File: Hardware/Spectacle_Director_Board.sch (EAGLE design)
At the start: 66 parts, among them J2 I2C-TRRS, J3 Serial-TRRS, Q1 310mA/60V/1.6Ω, Q2 310mA/60V/1.6Ω, U1 AP2151, U2 ATSAMD21G-A, U3 3.3V, U4 W25Q32FV

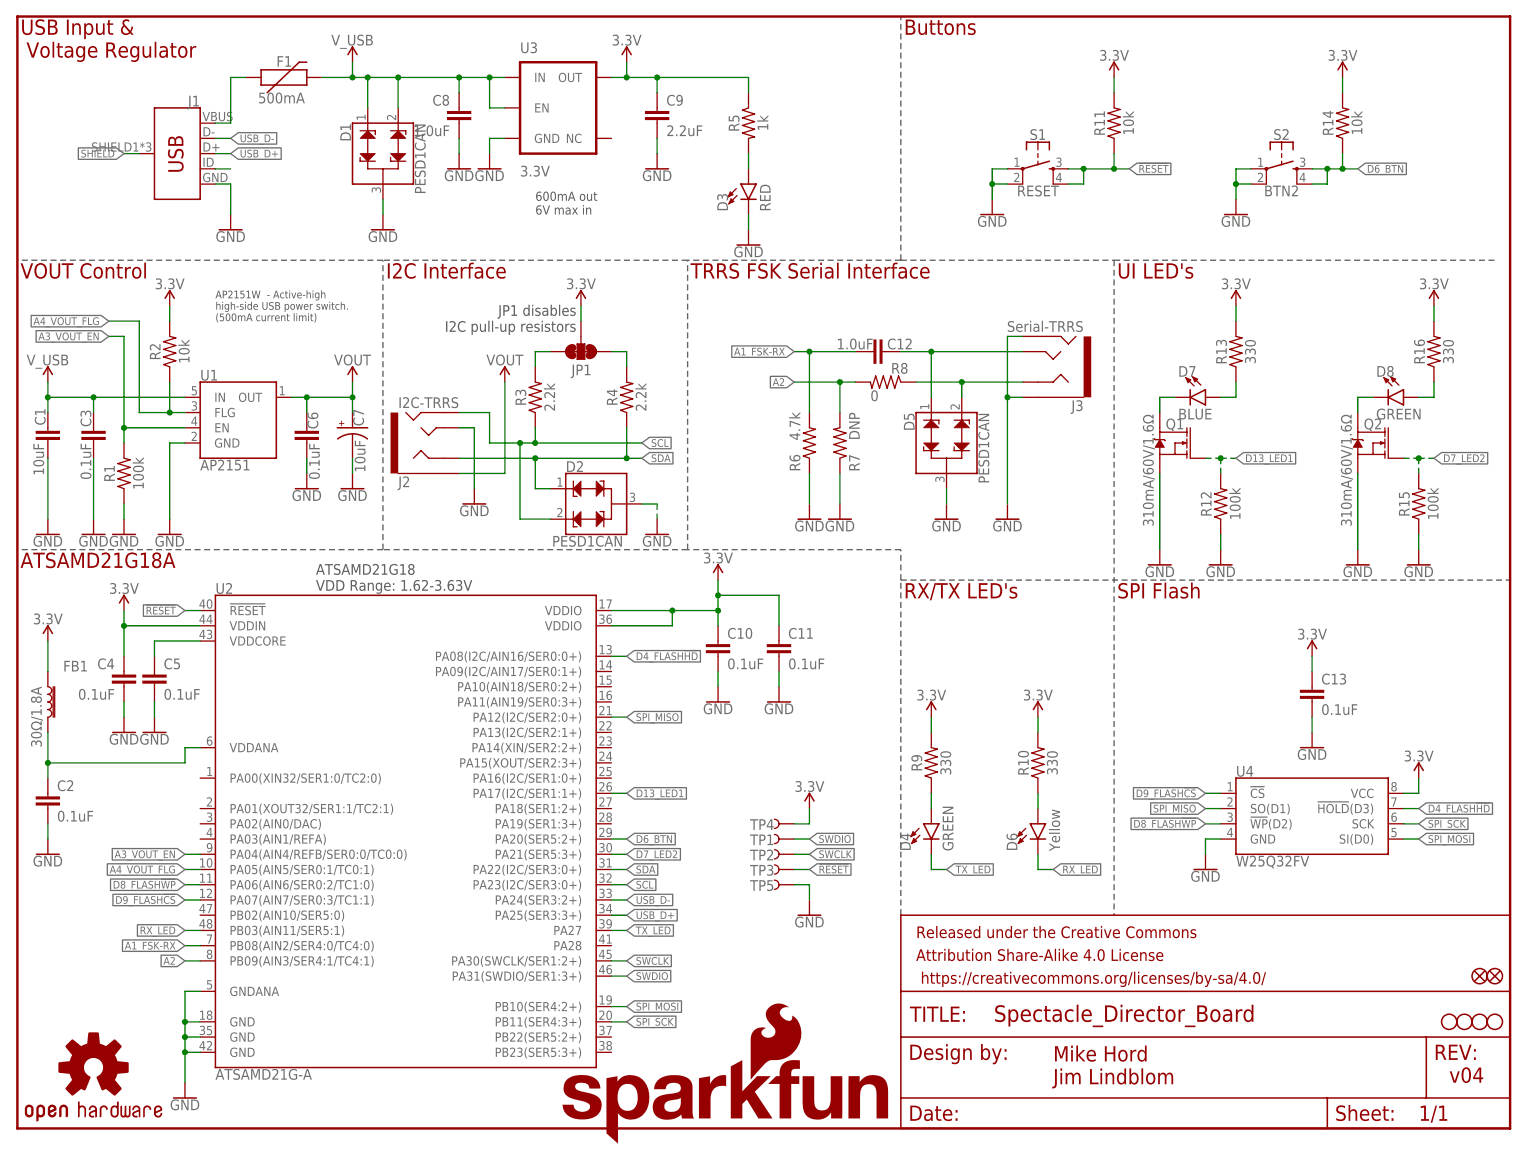
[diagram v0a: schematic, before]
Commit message: Added FSK demodulation hardware Changed pin assignment of FSK channel to channel with comparator Moved power switch FAULT line to a different pin
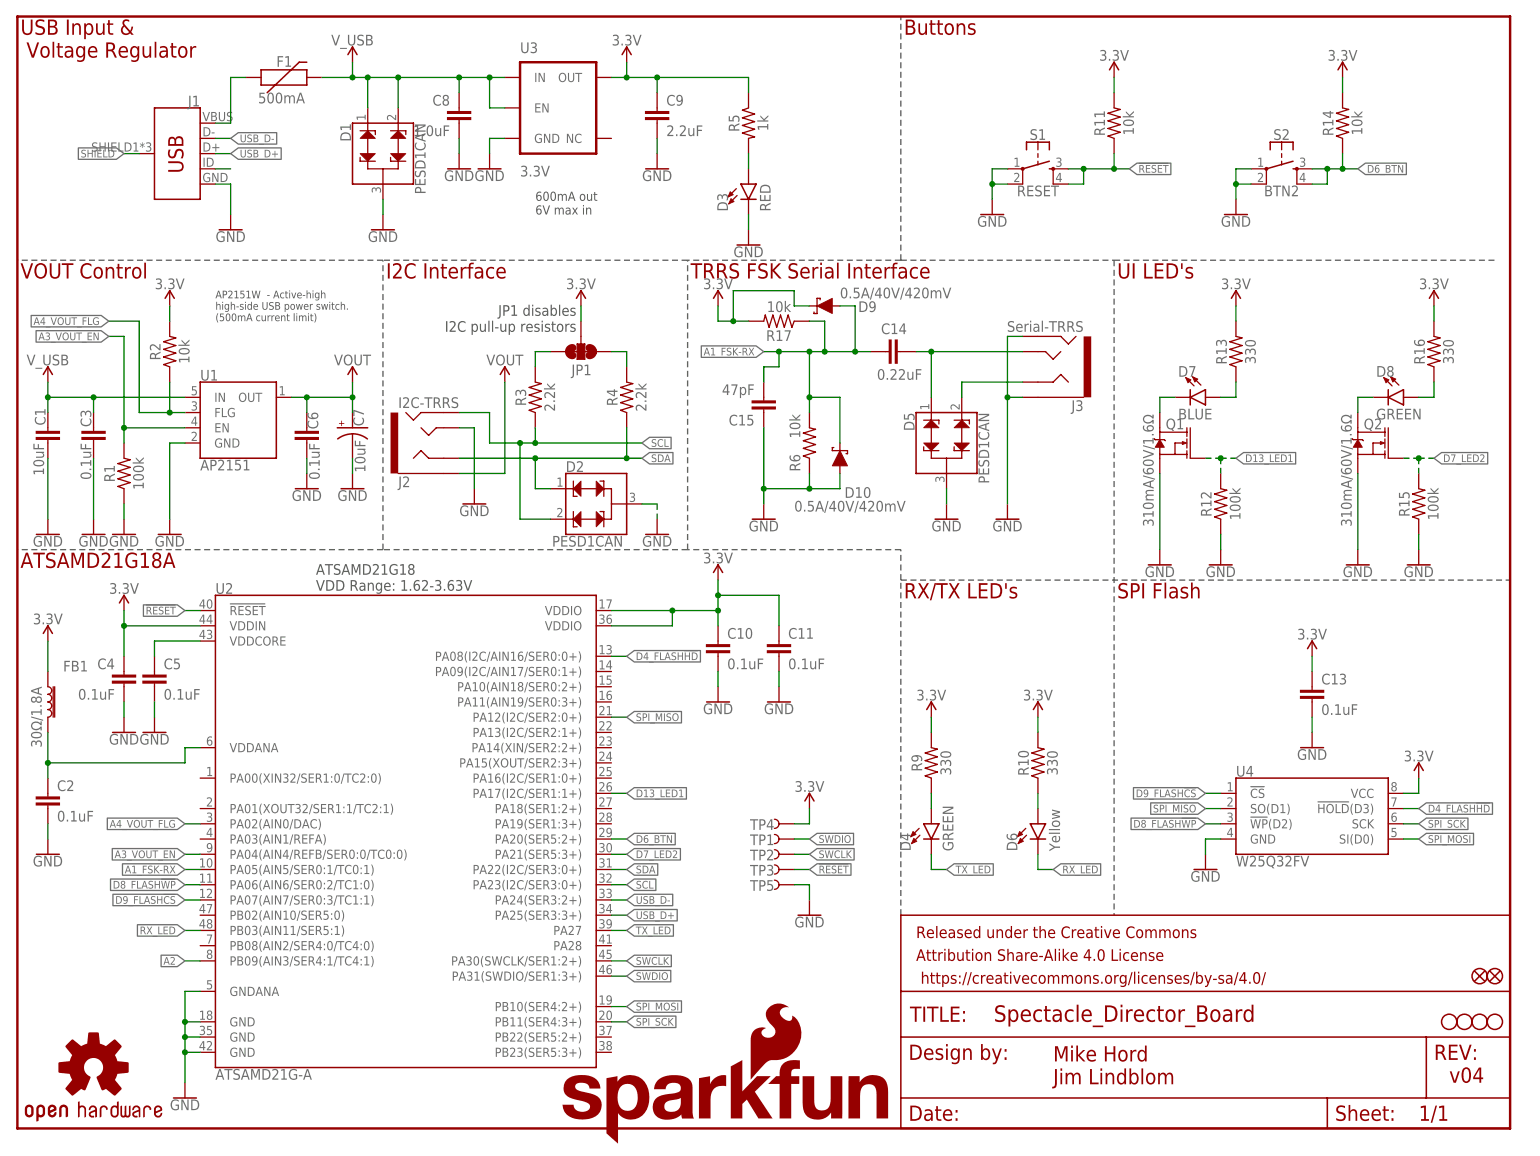
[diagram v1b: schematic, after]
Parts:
- removed C12: 1.0uF, SparkFun-Capacitors:1.0UF-0603-16V-10%
- removed R7: DNP, SparkFun-Resistors:4.7KOHM-0603-1/10W-1%
- removed R8: 0, SparkFun-Resistors:0OHM-0603-1/10W-5%
- added C14: 0.22uF, SparkFun-Capacitors:0.22UF-0603-25V-10%
- added C15: 47pF, SparkFun-Capacitors:47PF-0603-50V-5%
- added D10, D9: 0.5A/40V/420mV, SparkFun-DiscreteSemi:DIODE-SCHOTTKY-PMEG4005EJ
- added R17: 10k, SparkFun-Resistors:10KOHM-0603-1/10W-1%
- R6: value 4.7k -> 10k; device SparkFun-Resistors:4.7KOHM-0603-1/10W-1% -> SparkFun-Resistors:10KOHM-0603-1/10W-1%
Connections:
- net 3.3V: now also D9.C, R17.2
- net A1_FSK-RX: now also C14.1, C15.2, D10.C, D9.A, R17.1, U2.PA05(AIN5/SER0:1/TC0:1); no longer C12.2, U2.PB08(AIN2/SER4:0/TC4:0)
- net A2: no longer R7.2, R8.2
- net A4_VOUT_FLG: now also U2.PA02(AIN0/DAC); no longer U2.PA05(AIN5/SER0:1/TC0:1)
- net GND: now also C15.1, D10.A; no longer R7.1
- net RING1-RIGHT: no longer R8.1
- net TIP-LEFT: now also C14.2; no longer C12.1

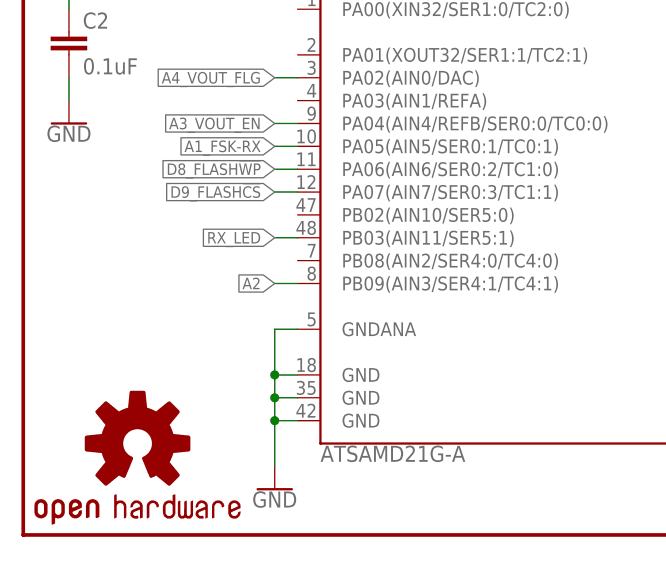
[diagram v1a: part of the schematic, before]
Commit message: FSK demodulation harware layout
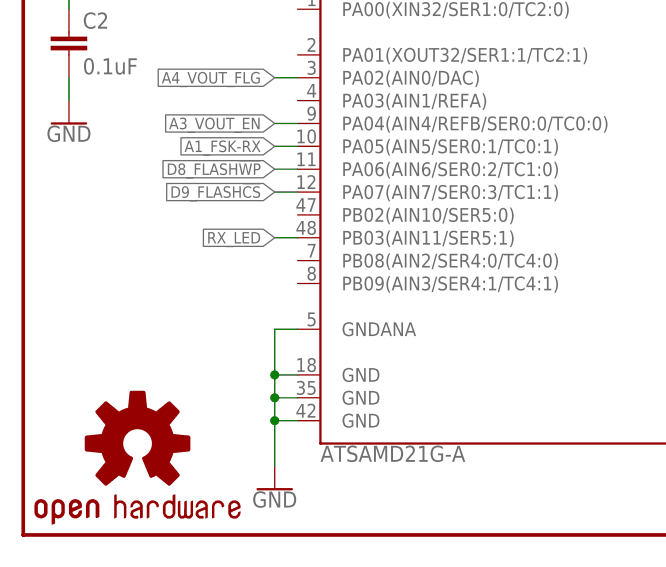
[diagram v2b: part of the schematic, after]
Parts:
- JP1: value JUMPER-SMT_3_2-NC_TRACE_SILK -> JUMPER-SMT_3_2-NC_TRACE_NO-SILK; device SparkFun-Jumpers:JUMPER-SMT_3_2-NC_TRACE_SILK -> SparkFun-Jumpers:JUMPER-SMT_3_2-NC_TRACE_NO-SILK
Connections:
- removed net A2: U2.PB09(AIN3/SER4:1/TC4:1)
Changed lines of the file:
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@@
 <grid distance="0.1" unitdist="inch" unit="inch" style="lines" multiple="1" display="no" altdistance="0.01" altunitdist="inch" altunit="inch"/>
 <layers>
-<layer number="1" name="Top" color="4" fill="1" visible="no" active="no"/>
-<layer number="2" name="Route2" color="1" fill="3" visible="no" active="no"/>
-<layer number="3" name="Route3" color="4" fill="3" visible="no" active="no"/>
-<layer number="4" name="Route4" color="1" fill="4" visible="no" active="no"/>
-<layer number="5" name="Route5" color="4" fill="4" visible="no" active="no"/>
-<layer number="6" name="Route6" color="1" fill="8" visible="no" active="no"/>
-<layer number="7" name="Route7" color="4" fill="8" visible="no" active="no"/>
-<layer number="8" name="Route8" color="1" fill="2" visible="no" active="no"/>
-<layer number="9" name="Route9" color="4" fill="2" visible="no" active="no"/>
-<layer number="10" name="Route10" color="1" fill="7" visible="no" active="no"/>
-<layer number="11" name="Route11" color="4" fill="7" visible="no" active="no"/>
-<layer number="12" name="Route12" color="1" fill="5" visible="no" active="no"/>
-<layer number="13" name="Route13" color="4" fill="5" visible="no" active="no"/>
-<layer number="14" name="Route14" color="1" fill="6" visible="no" active="no"/>
-<layer number="15" name="Route15" color="4" fill="6" visible="no" active="no"/>
-<layer number="16" name="Bottom" color="1" fill="1" visible="no" active="no"/>
-<layer number="17" name="Pads" color="2" fill="1" visible="no" active="no"/>
-<layer number="18" name="Vias" color="2" fill="1" visible="no" active="no"/>
-<layer number="19" name="Unrouted" color="6" fill="1" visible="no" active="no"/>
-<layer number="20" name="Dimension" color="15" fill="1" visible="no" active="no"/>
-<layer number="21" name="tPlace" color="16" fill="1" visible="no" active="no"/>
-<layer number="22" name="bPlace" color="14" fill="1" visible="no" active="no"/>
-<layer number="23" name="tOrigins" color="15" fill="1" visible="no" active="no"/>
-<layer number="24" name="bOrigins" color="15" fill="1" visible="no" active="no"/>
-<layer number="25" name="tNames" color="7" fill="1" visible="no" active="no"/>
-<layer number="26" name="bNames" color="7" fill="1" visible="no" active="no"/>
-<layer number="27" name="tValues" color="7" fill="1" visible="no" active="no"/>
-<layer number="28" name="bValues" color="7" fill="1" visible="no" active="no"/>
+<layer number="1" name="Top" color="4" fill="1" visible="yes" active="no"/>
+<layer number="2" name="Route2" color="1" fill="3" visible="yes" active="no"/>
+<layer number="3" name="Route3" color="4" fill="3" visible="yes" active="no"/>
+<layer number="4" name="Route4" color="1" fill="4" visible="yes" active="no"/>
+<layer number="5" name="Route5" color="4" fill="4" visible="yes" active="no"/>
+<layer number="6" name="Route6" color="1" fill="8" visible="yes" active="no"/>
+<layer number="7" name="Route7" color="4" fill="8" visible="yes" active="no"/>
+<layer number="8" name="Route8" color="1" fill="2" visible="yes" active="no"/>
+<layer number="9" name="Route9" color="4" fill="2" visible="yes" active="no"/>
+<layer number="10" name="Route10" color="1" fill="7" visible="yes" active="no"/>
+<layer number="11" name="Route11" color="4" fill="7" visible="yes" active="no"/>
+<layer number="12" name="Route12" color="1" fill="5" visible="yes" active="no"/>
+<layer number="13" name="Route13" color="4" fill="5" visible="yes" active="no"/>
+<layer number="14" name="Route14" color="1" fill="6" visible="yes" active="no"/>
+<layer number="15" name="Route15" color="4" fill="6" visible="yes" active="no"/>
+<layer number="16" name="Bottom" color="1" fill="1" visible="yes" active="no"/>
+<layer number="17" name="Pads" color="2" fill="1" visible="yes" active="no"/>
+<layer number="18" name="Vias" color="2" fill="1" visible="yes" active="no"/>
+<layer number="19" name="Unrouted" color="6" fill="1" visible="yes" active="no"/>
+<layer number="20" name="Dimension" color="15" fill="1" visible="yes" active="no"/>
+<layer number="21" name="tPlace" color="16" fill="1" visible="yes" active="no"/>
+<layer number="22" name="bPlace" color="14" fill="1" visible="yes" active="no"/>
+<layer number="23" name="tOrigins" color="15" fill="1" visible="yes" active="no"/>
+<layer number="24" name="bOrigins" color="15" fill="1" visible="yes" active="no"/>
+<layer number="25" name="tNames" color="7" fill="1" visible="yes" active="no"/>
+<layer number="26" name="bNames" color="7" fill="1" visible="yes" active="no"/>
+<layer number="27" name="tValues" color="7" fill="1" visible="yes" active="no"/>
+<layer number="28" name="bValues" color="7" fill="1" visible="yes" active="no"/>
 <layer number="29" name="tStop" color="7" fill="3" visible="no" active="no"/>
 <layer number="30" name="bStop" color="7" fill="6" visible="no" active="no"/>
@@
 <layer number="35" name="tGlue" color="7" fill="4" visible="no" active="no"/>
 <layer number="36" name="bGlue" color="7" fill="5" visible="no" active="no"/>
-<layer number="37" name="tTest" color="7" fill="1" visible="no" active="no"/>
-<layer number="38" name="bTest" color="7" fill="1" visible="no" active="no"/>
+<layer number="37" name="tTest" color="7" fill="1" visible="yes" active="no"/>
+<layer number="38" name="bTest" color="7" fill="1" visible="yes" active="no"/>
 <layer number="39" name="tKeepout" color="16" fill="11" visible="no" active="no"/>
 <layer number="40" name="bKeepout" color="1" fill="11" visible="no" active="no"/>
@@
 <layer number="44" name="Drills" color="7" fill="1" visible="no" active="no"/>
 <layer number="45" name="Holes" color="7" fill="1" visible="no" active="no"/>
-<layer number="46" name="Milling" color="3" fill="1" visible="no" active="no"/>
-<layer number="47" name="Measures" color="7" fill="1" visible="no" active="no"/>
-<layer number="48" name="Document" color="7" fill="1" visible="no" active="no"/>
-<layer number="49" name="Reference" color="7" fill="1" visible="no" active="no"/>
-<layer number="50" name="dxf" color="7" fill="1" visible="no" active="no"/>
-<layer number="51" name="tDocu" color="6" fill="1" visible="no" active="no"/>
-<layer number="52" name="bDocu" color="7" fill="1" visible="no" active="no"/>
-<layer number="53" name="tGND_GNDA" color="7" fill="9" visible="no" active="no"/>
-<layer number="54" name="bGND_GNDA" color="1" fill="9" visible="no" active="no"/>
-<layer number="56" name="wert" color="7" fill="1" visible="no" active="no"/>
-<layer number="57" name="tCAD" color="7" fill="1" visible="no" active="no"/>
-<layer number="59" name="tCarbon" color="7" fill="1" visible="no" active="no"/>
-<layer number="60" name="bCarbon" color="7" fill="1" visible="no" active="no"/>
+<layer number="46" name="Milling" color="3" fill="1" visible="yes" active="no"/>
+<layer number="47" name="Measures" color="7" fill="1" visible="yes" active="no"/>
+<layer number="48" name="Document" color="7" fill="1" visible="yes" active="no"/>
+<layer number="49" name="Reference" color="7" fill="1" visible="yes" active="no"/>
+<layer number="50" name="dxf" color="7" fill="1" visible="yes" active="no"/>
+<layer number="51" name="tDocu" color="6" fill="1" visible="yes" active="no"/>
+<layer number="52" name="bDocu" color="7" fill="1" visible="yes" active="no"/>
+<layer number="53" name="tGND_GNDA" color="7" fill="9" visible="yes" active="no"/>
+<layer number="54" name="bGND_GNDA" color="1" fill="9" visible="yes" active="no"/>
+<layer number="56" name="wert" color="7" fill="1" visible="yes" active="no"/>
+<layer number="57" name="tCAD" color="7" fill="1" visible="yes" active="no"/>
+<layer number="59" name="tCarbon" color="7" fill="1" visible="yes" active="no"/>
+<layer number="60" name="bCarbon" color="7" fill="1" visible="yes" active="no"/>
 <layer number="90" name="Modules" color="5" fill="1" visible="yes" active="yes"/>
 <layer number="91" name="Nets" color="2" fill="1" visible="yes" active="yes"/>
@@
 <part name="R3" library="SparkFun-Resistors" deviceset="2.2KOHM" device="-0603-1/10W-1%" value="2.2k"/>
 <part name="R4" library="SparkFun-Resistors" deviceset="2.2KOHM" device="-0603-1/10W-1%" value="2.2k"/>
-<part name="JP1" library="SparkFun-Jumpers" deviceset="JUMPER-SMT_3_2-NC_TRACE" device="_SILK"/>
+<part name="JP1" library="SparkFun-Jumpers" deviceset="JUMPER-SMT_3_2-NC_TRACE" device="_NO-SILK" value="JUMPER-SMT_3_2-NC_TRACE_NO-SILK"/>
 <part name="SUPPLY8" library="SparkFun-PowerSymbols" deviceset="3.3V" device=""/>
 <part name="D2" library="SparkFun-DiscreteSemi" deviceset="PESD1CAN" device=""/>
@@
 </segment>
 </net>
-<net name="A2" class="0">
-<segment>
-<pinref part="U2" gate="G$1" pin="PB09(AIN3/SER4:1/TC4:1)"/>
-<wire x1="30.48" y1="27.94" x2="27.94" y2="27.94" width="0.1524" layer="91"/>
-<label x="27.94" y="27.94" size="1.27" layer="95" rot="R180" xref="yes"/>
-</segment>
-</net>
 <net name="D4_FLASH!HD!" class="0">
 <segment>
@@
 <net name="A4_VOUT_FLG" class="0">
 <segment>
+<pinref part="U2" gate="G$1" pin="PA02(AIN0/DAC)"/>
+<wire x1="30.48" y1="50.8" x2="27.94" y2="50.8" width="0.1524" layer="91"/>
+<label x="27.94" y="50.8" size="1.27" layer="95" rot="R180" xref="yes"/>
+</segment>
+<segment>
 <pinref part="U1" gate="G$1" pin="FLG"/>
 <wire x1="27.94" y1="119.38" x2="25.4" y2="119.38" width="0.1524" layer="91"/>
@@
 <junction x="25.4" y="119.38"/>
 </segment>
-<segment>
-<pinref part="U2" gate="G$1" pin="PA02(AIN0/DAC)"/>
-<wire x1="30.48" y1="50.8" x2="27.94" y2="50.8" width="0.1524" layer="91"/>
-<label x="27.94" y="50.8" size="1.27" layer="95" rot="R180" xref="yes"/>
-</segment>
-</net>
+</net>
